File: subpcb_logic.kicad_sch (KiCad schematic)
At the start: 66 parts, among them J1 Conn_01x04, J11 Conn_01x05, J12 xcore, J13 Screw_Terminal_01x02, J14 Conn_01x02, J15 Conn_01x04, J16 Conn_01x05, J20 Conn_01x05, J21 Conn_01x05, J23 Conn_01x05, J24 Conn_01x02, J28 Conn_01x03_Male, J30 Conn_01x03_Male, J31 Conn_01x03_Pin, J32 Conn_01x05_Pin, J5 Conn_02x08_Odd_Even, J52 Conn_01x03_Male, J54 Conn_01x03_Male, M1 Fan, Q1 AO3400A, Q2 AO3400A, U5 M24C02-WMN, U6 AS-RTK2B-MICRO-F9P-L1L2SMATH-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, U7 TXS0108EPW

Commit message: Routing progress and vertical USB
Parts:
- added J45: RJ12, 855135002:CONN_85513-5002_MOL, symbol Connector:RJ12
- added J48: RJ45, RF45:RJ45_Molex_0855135013_Vertical, symbol Connector:RJ45
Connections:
- net 5V: now also J45.1, J45.3, J48.4, J48.6
- net GND: now also J45.2, J48.5
- net HALL0_5V: now also J45.6
- net HALL1_5V: now also J48.1
- net HALL2_5V: now also J48.3

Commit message: Incremental routing updates
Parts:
- removed J11, J20, J21: Conn_01x05, Connector_JST:JST_XH_B5B-XH-A_1x05_P2.50mm_Vertical, symbol Connector_Generic:Conn_01x05

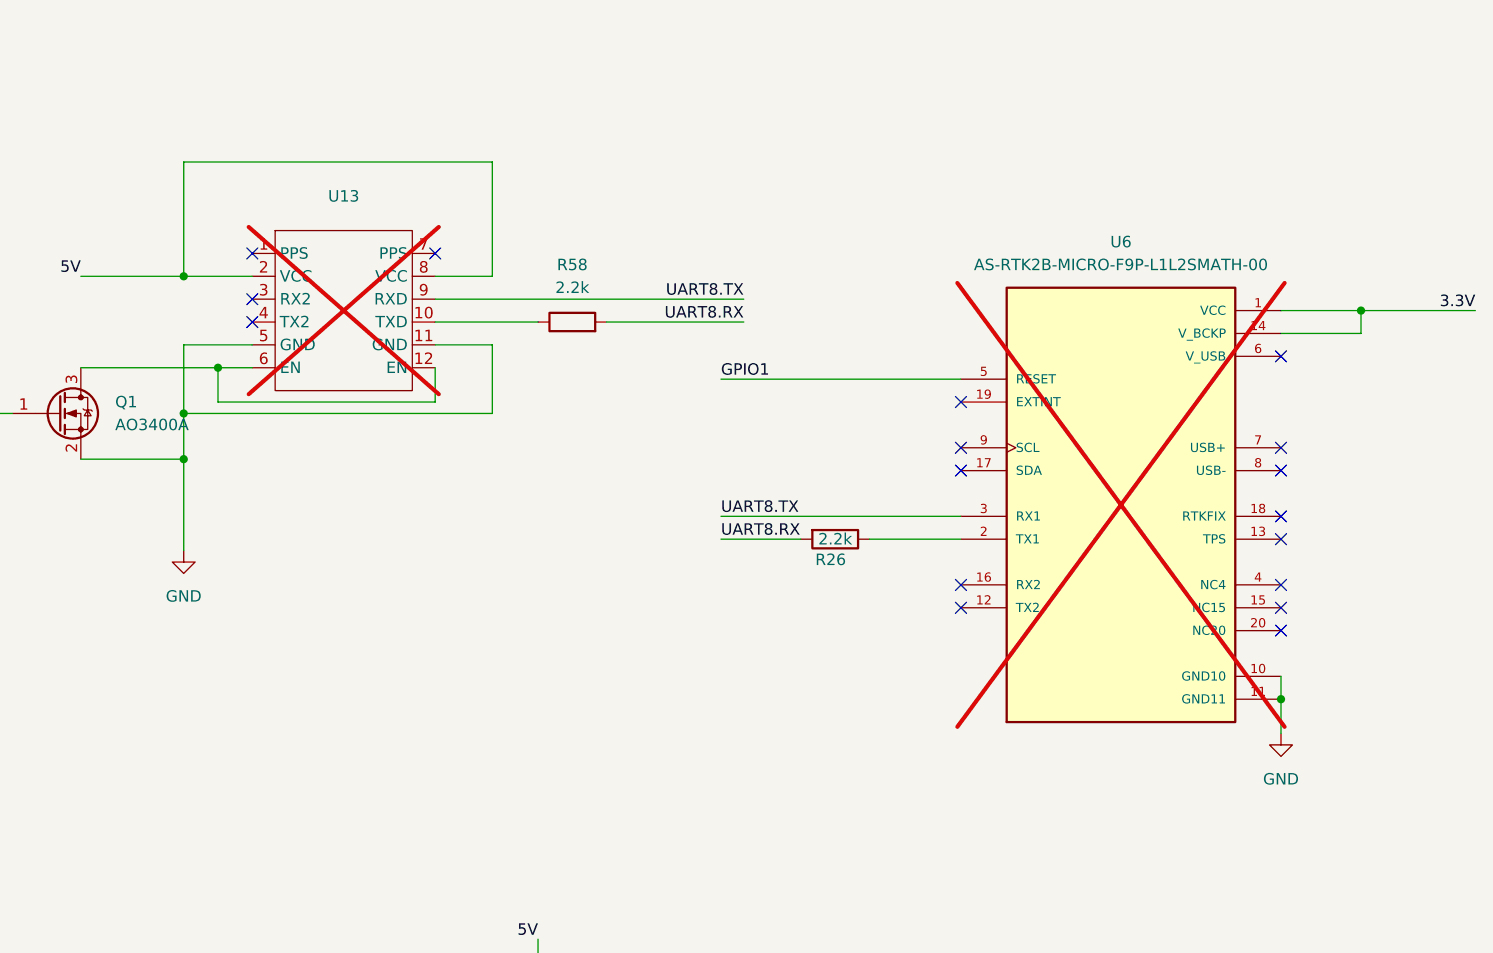
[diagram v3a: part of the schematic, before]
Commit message: Additional routing
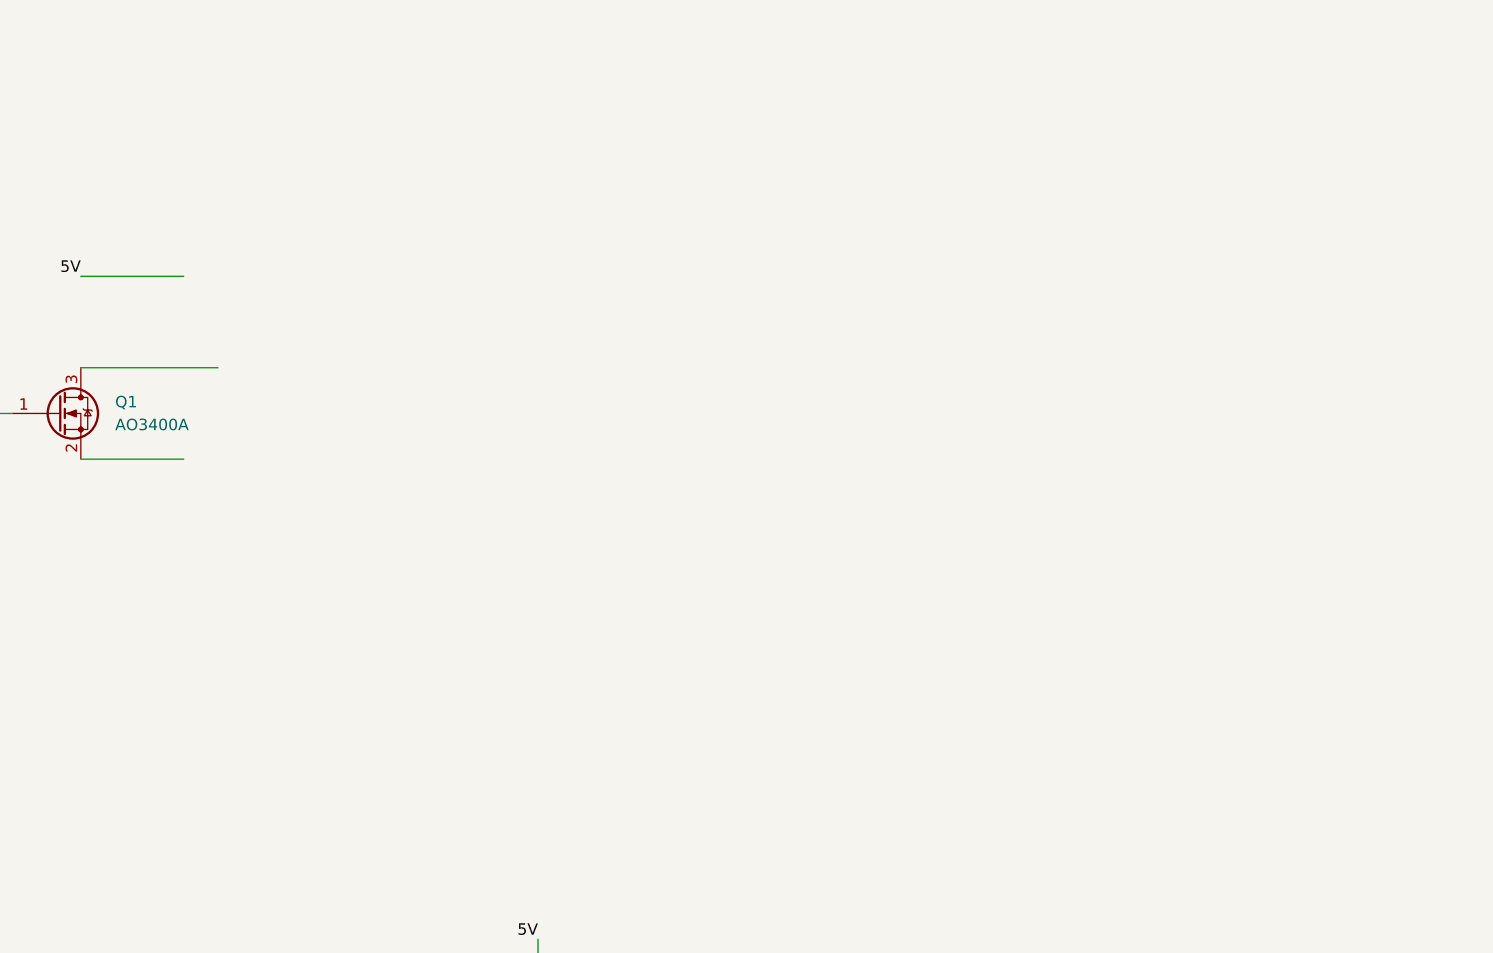
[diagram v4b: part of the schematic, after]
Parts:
- removed R26, R58: 2.2k, Resistor_SMD:R_0805_2012Metric, symbol Device:R
- removed U13: ~, xtech:UM9XX_WitMotion, symbol xtech:UM9xx_WitMotion
- removed U6: AS-RTK2B-MICRO-F9P-L1L2SMATH-00, local_GPS:MODULE_AS-RTK2B-MICRO-F9P-L1L2SMATH-00, symbol local_GPS:AS-RTK2B-MICRO-F9P-L1L2SMATH-00
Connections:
- net GND: no longer Q1.2 (S)
- no-connect marks 60 -> 43

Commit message: Further routing progress
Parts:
- removed J28, J52: Conn_01x03_Male, Connector_PinHeader_2.54mm:PinHeader_1x03_P2.54mm_Vertical, symbol Connector:Conn_01x03_Male
- removed Q1: AO3400A, Package_TO_SOT_SMD:SOT-23, symbol Transistor_FET:BSS138
- removed R24: 10k, Resistor_SMD:R_0805_2012Metric_Pad1.20x1.40mm_HandSolder, symbol Device:R
- removed R25: 150R, Resistor_SMD:R_0805_2012Metric_Pad1.20x1.40mm_HandSolder, symbol Device:R
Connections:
- net 5V: no longer J30.3 (Pin_3), J54.3 (Pin_3)
- net HALL0_5V: now also J30.2 (Pin_2); no longer J54.2 (Pin_2)
- net HALL1_5V: now also J30.3 (Pin_3)
- net HALL2_5V: now also J54.2 (Pin_2); no longer J30.2 (Pin_2)
- new net DEBUG_NC: J54.3 (Pin_3)
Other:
- moved on the sheet: J30, J54
